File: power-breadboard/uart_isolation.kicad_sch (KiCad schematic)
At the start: 9 parts, among them J11 Screw_Terminal_01x04, U22 ADUM1201AR, U23 SRV05-4

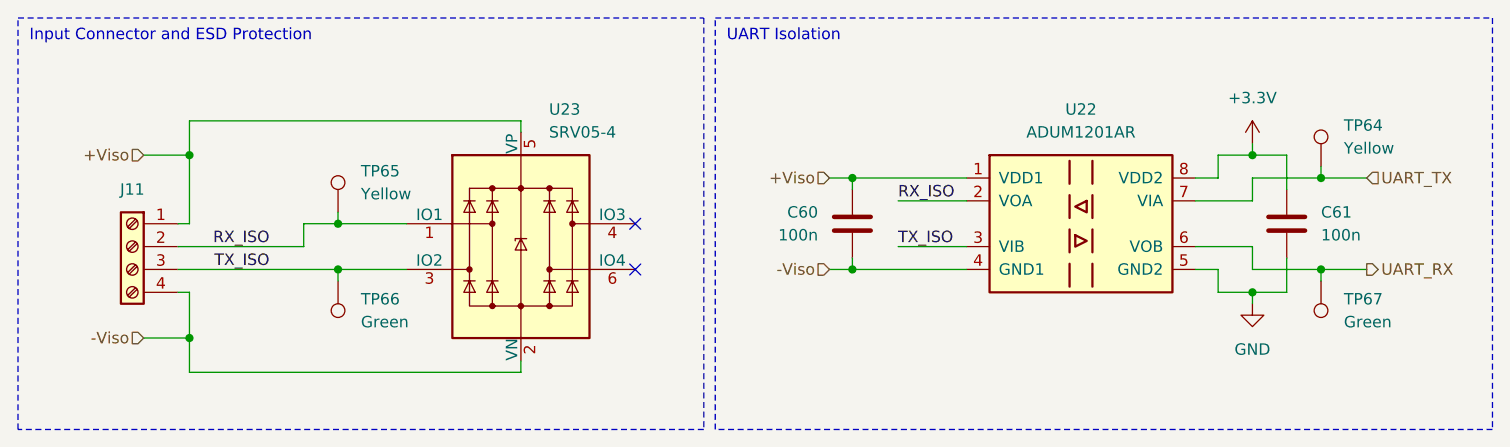
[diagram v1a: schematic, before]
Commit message: power-breadboard: finish isolated interfaces
Replaced UART isolators with discrete optocouplers.
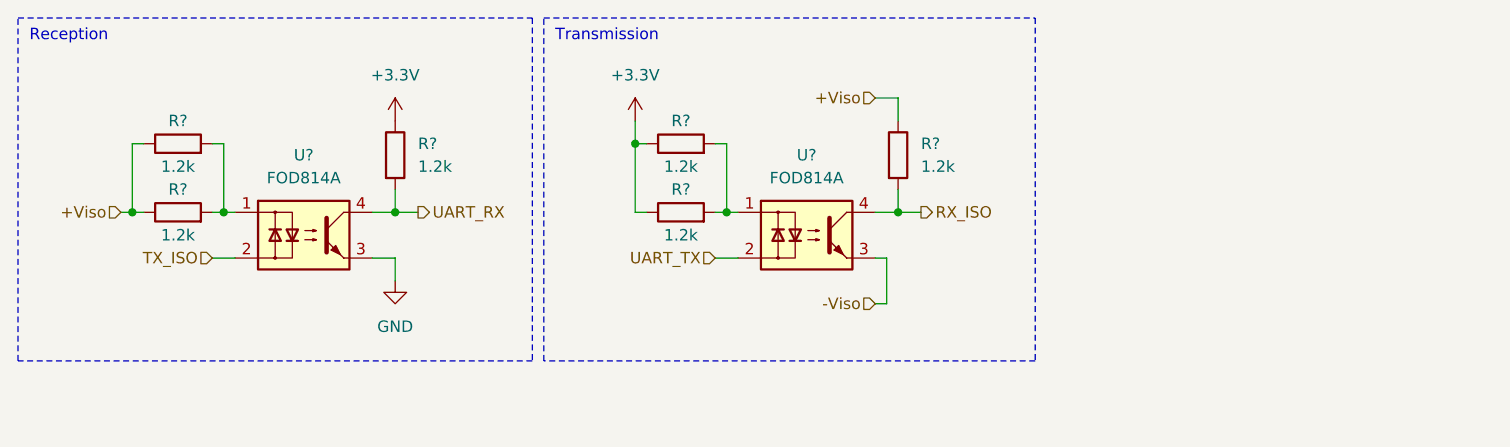
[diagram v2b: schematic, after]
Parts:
- removed C60, C61: 100n, Capacitor_SMD:C_0402_1005Metric_Pad0.74x0.62mm_HandSolder, symbol Device:C
- removed J11: Screw_Terminal_01x04, Exocet:Wuerth_Term_Blk_4pos_Side_Entry_5mm, symbol Connector:Screw_Terminal_01x04
- removed TP64, TP65: Yellow, TestPoint:TestPoint_Keystone_5005-5009_Compact, symbol Connector:TestPoint
- removed TP66, TP67: Green, TestPoint:TestPoint_Keystone_5005-5009_Compact, symbol Connector:TestPoint
- removed U22: ADUM1201AR, Package_SO:SOIC-8_3.9x4.9mm_P1.27mm, symbol Isolator:ADuM1201AR
- removed U23: SRV05-4, Package_TO_SOT_SMD:SOT-23-6, symbol Power_Protection:SRV05-4
- added R? (x6): 1.2k, symbol Device:R
- added U? (x2): FOD814A, Package_SO:SOP-4_4.4x2.6mm_P1.27mm, symbol Isolator:FODM214A
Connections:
- net +3.3V: now also R?.1, R?.1, R?.1
- net +Viso: now also R?.1, R?.1, R?.1
- net -Viso: now also U?.3
- net GND: now also U?.3
- net RX_ISO: now also R?.2, U?.4
- net TX_ISO: now also U?.2
- net UART_RX: now also R?.2, U?.4
- net UART_TX: now also U?.2
- new net: R?.2, R?.2, U?.1 (x2)
- no-connect marks 2 -> 0
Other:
- note added: "Reception"
- note added: "Transmission"
- note removed: "Input Connector and ESD Protection"
- note removed: "UART Isolation"
